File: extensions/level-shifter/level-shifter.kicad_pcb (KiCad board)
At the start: 2 copper layers, 59.1 x 32.4 mm, 61 parts, among them P1 CONN_01X03, P10 CONN_02X05, P2 CONN_01X03, P3 CONN_01X03, P4 CONN_01X03, P5 CONN_01X03, P6 CONN_01X03, P7 CONN_01X03, P8 CONN_01X02, P9 CONN_02X05, Q1 FDN339AN, Q10 FDN339AN, Q11 SI2301, Q12 FDN339AN, Q13 FDN339AN, Q14 FDN339AN, Q15 FDN339AN, Q16 SI2301, Q17 FDN339AN, Q18 SI2301, Q19 FDN339AN, Q2 FDN339AN, Q20 SI2301, Q21 FDN339AN, Q3 FDN339AN, Q4 FDN339AN, Q5 SI2301, Q6 FDN339AN, Q7 SI2301, Q8 FDN339AN, Q9 SI2301

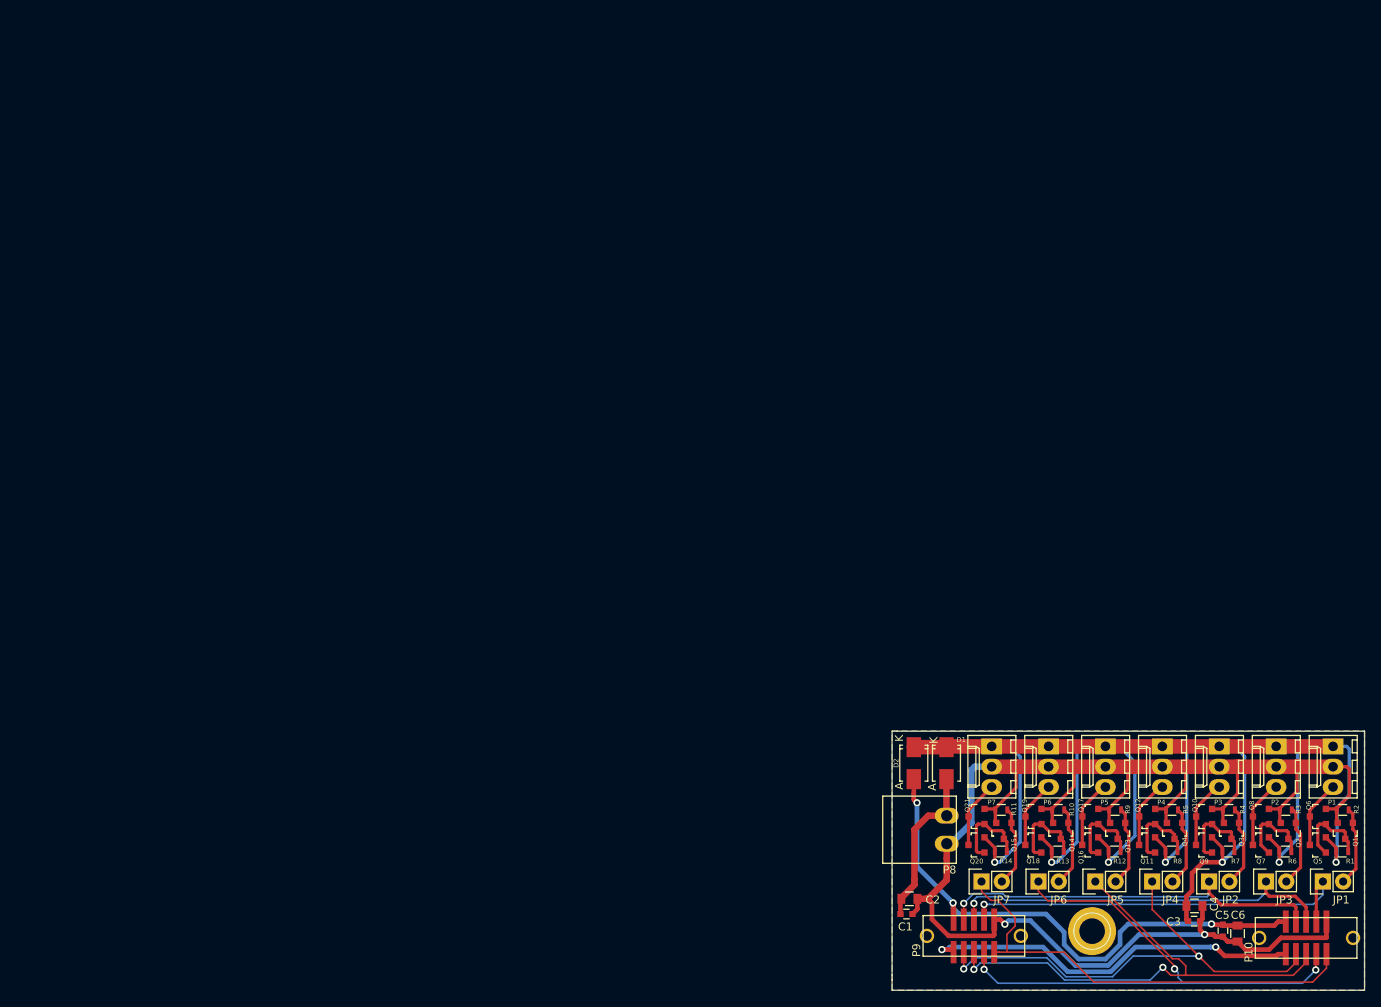
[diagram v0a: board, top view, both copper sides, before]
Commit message: Redesigned for SMD jumpers
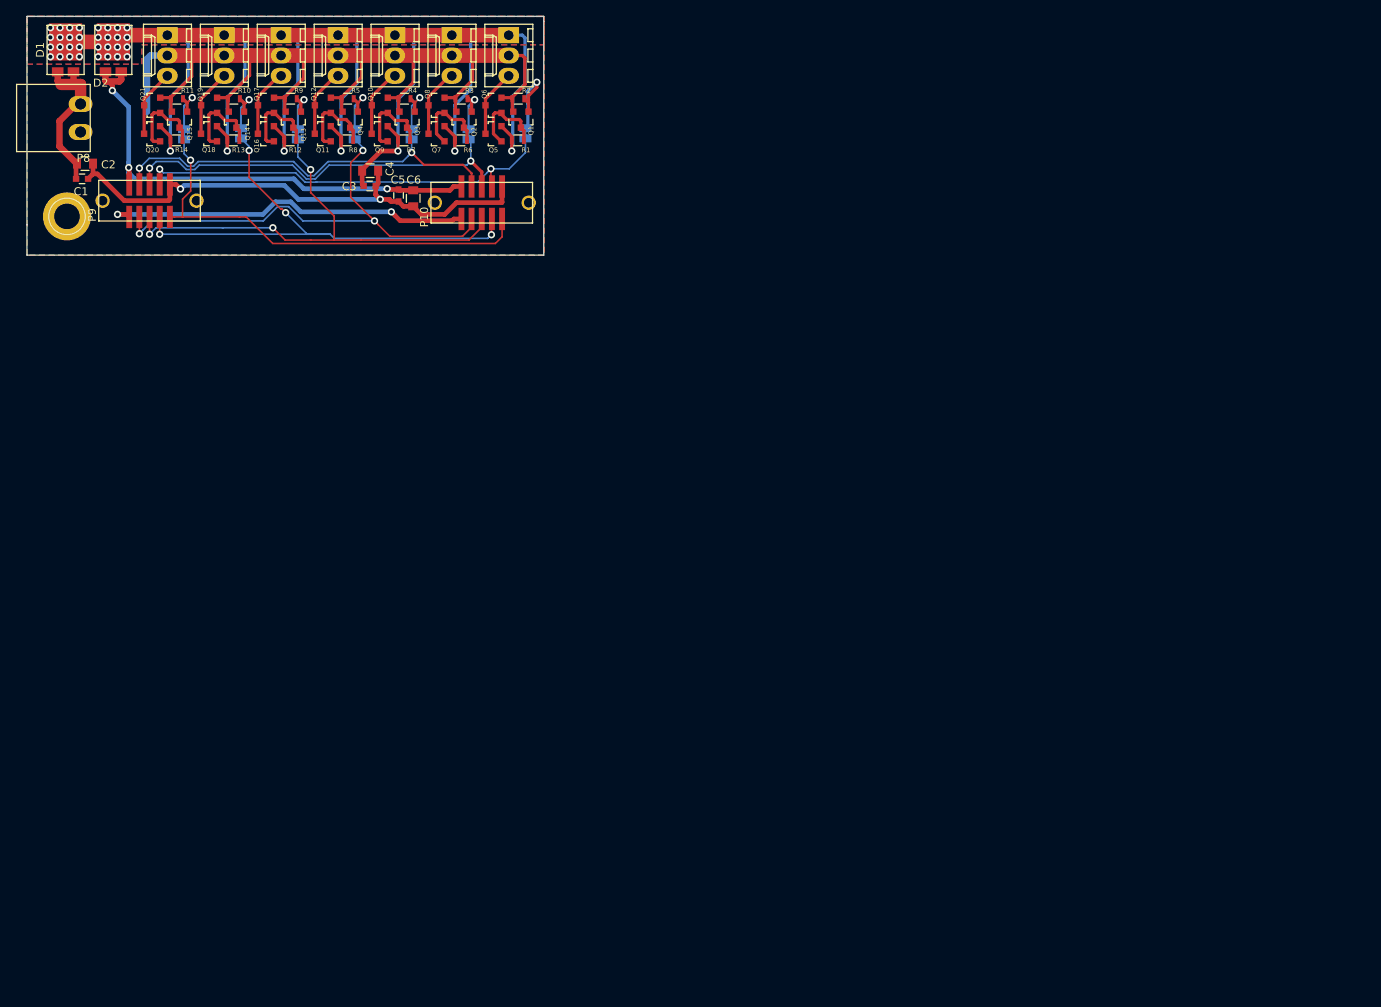
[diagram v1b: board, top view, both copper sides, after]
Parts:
- D1, D2: value D_Small -> FSV12120V; footprint Diodes_SMD:SMA_Standard -> Diodes:TO-277_3L
- JP1, JP2, JP3, JP4, JP5, JP6, JP7: footprint Pin_Headers:Pin_Header_Straight_1x02 -> Jumpers:Solder-jumper-NC; moved to B.Cu
- P6: footprint Molex_KK_6410-03 -> Connectors:Molex_KK_6410-03
- P7: footprint Connectors_Molex:Molex_KK_6410-03 -> Connectors:Molex_KK_6410-03
- P9: footprint SHF-105-01-L-D-SM-LC -> Connectors:SHF-105-01-L-D-SM-LC
- moved 5,5 156.2 mm to (5.00, 25.0)
- moved D1 141.7 mm to (4.83, 4.19)
- moved P8 140.1 mm to (3.30, 12.7)
- moved C5 138.1 mm to (46.4, 22.4)
- moved C6 138.1 mm to (48.3, 22.7)
- moved P10 138.1 mm to (56.8, 23.3)
- moved P9 138.1 mm to (15.3, 23.0)
- moved C1 138.1 mm to (6.89, 20.3)
- moved C2 138.1 mm to (7.25, 18.4)
- moved C3 138.1 mm to (42.8, 21.2)
- moved C4 138.1 mm to (42.9, 19.3)
- moved JP1 136.7 mm to (62.3, 14.6)
- moved JP6 136.7 mm to (26.7, 14.6)
- moved JP4 136.6 mm to (41.0, 14.7)
- moved JP5 136.6 mm to (33.9, 14.7)
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- renumbered 25,25 to 5,5
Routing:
- net GPIO5: track 87.6 -> 65.5 mm, vias 3 -> 4
- net GND: track 203.7 -> 185.4 mm
- net +5V: track 68.4 -> 61.7 mm
- net VDD: track 217.2 -> 212.3 mm, vias 7 -> 39
- net Net-(JP2-Pad2): track 10.2 -> 6.40 mm, vias 0 -> 1
- net GPIO3: track 64.5 -> 60.8 mm, vias 2 -> 3
- net Net-(JP5-Pad2): track 10.0 -> 6.38 mm, vias 0 -> 1
- net Net-(JP6-Pad2): track 10.1 -> 6.67 mm, vias 0 -> 1
- net Net-(JP3-Pad2): track 10.1 -> 7.10 mm, vias 0 -> 1
- net Net-(JP4-Pad2): track 10.1 -> 7.10 mm, vias 0 -> 1
- net Net-(JP7-Pad2): track 10.1 -> 7.10 mm, vias 0 -> 1
- net GPIO6: track 51.8 -> 54.3 mm, vias 1 -> 2
- net +3V3: track 47.8 -> 46.3 mm
- net GPIO4: track 50.1 -> 51.4 mm, vias 1 -> 2
- net Net-(JP1-Pad2): track 9.98 -> 11.1 mm, vias 0 -> 1
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- added copper zone on B.Cu, net VDD
- added copper zone on F.Cu, net VDD
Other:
- board size 59.1 x 32.4 mm -> 64.6 x 29.8 mm
- board text added: "Cut jumpers to deactivate output"
- board text removed: "Use jumpers to activate output"
